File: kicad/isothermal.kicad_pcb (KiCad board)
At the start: 2 copper layers, 62.2 x 49.9 mm, 39 parts, among them P10 CONN_2X1, P40 CONN_2X1, P41 CONN_2X1, P60 CONN_2X1, P70 CONN_6X1, P71 CONN_8X1, P72 CONN_10X1, P73 CONN_8X1, Q1 2N3904, U1 LM324

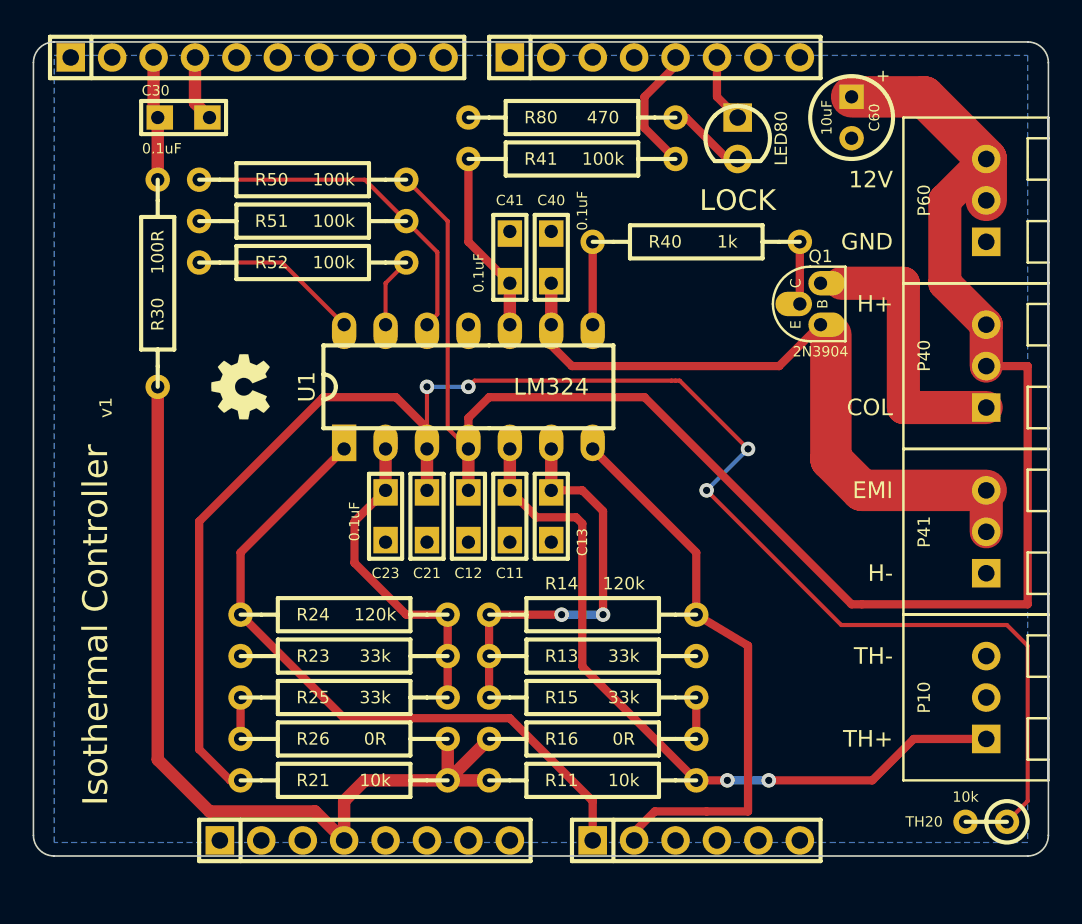
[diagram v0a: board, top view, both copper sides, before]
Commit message: increasing terminal block hole size, fixing pin spacing
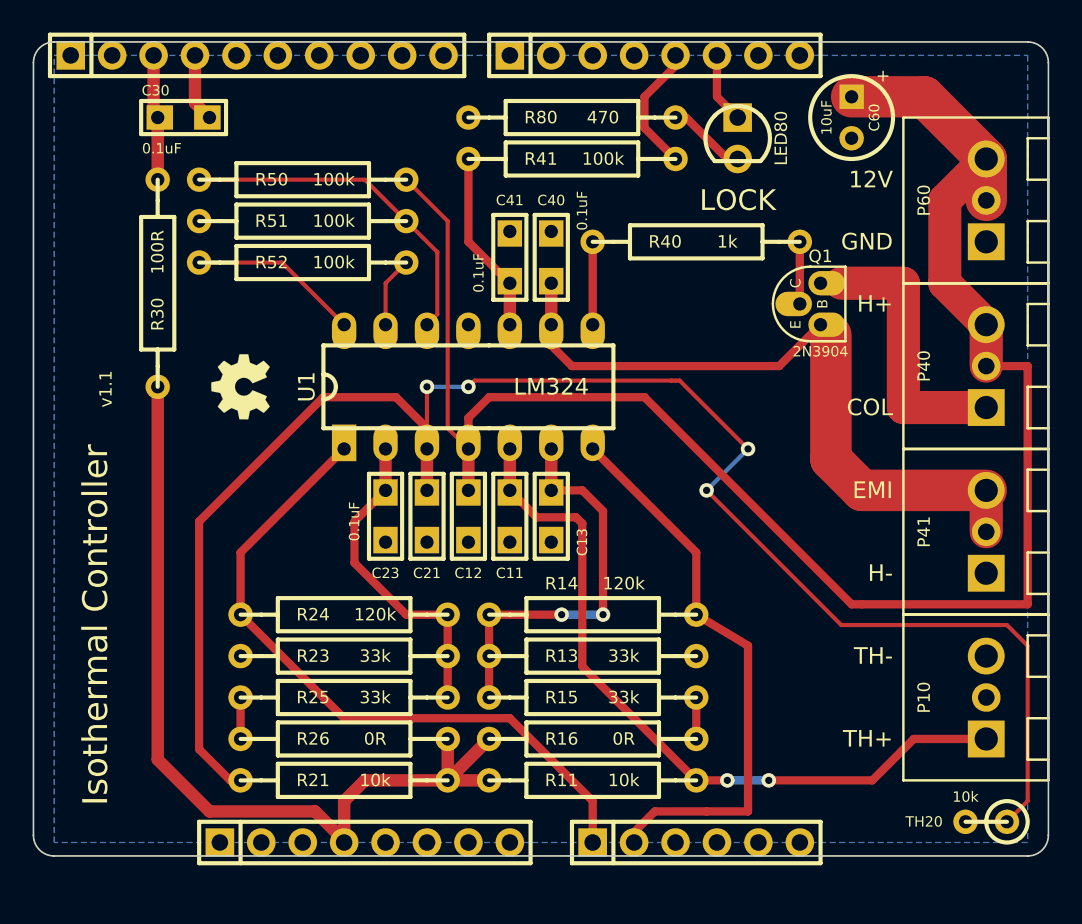
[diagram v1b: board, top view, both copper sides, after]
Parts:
- moved P70 0.13 mm to (210.8, 172.7)
- moved P71 0.13 mm to (188.0, 172.7)
- moved P72 0.13 mm to (178.8, 124.5)
- moved P73 0.13 mm to (205.7, 124.5)
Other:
- board text added: "v1.1"
- board text removed: "v1"

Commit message: v1.1
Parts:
- removed C41: 0.1uF, CERCAP_15_059B_0805
- removed R50, R51, R52: 100k, R_AXIAL_0W25_059A_05_PL
- added C44: 0.1uF, CERCAP_15_059B_0805, F.Cu at (200.7, 127.6)
- added D30: ZENER, DIODE_SS_059A_03_PL, F.Cu at (182.2, 132.1)
- added R31: 330R, R_AXIAL_0W25_059A_PL, F.Cu at (181.0, 146.7)
- added R42: 10k, R_AXIAL_0W25_059A_PL, F.Cu at (189.2, 135.9)
- added R43: 1k, R_AXIAL_0W25_059A_PL, F.Cu at (199.4, 130.8)
- added R44: 100k, R_AXIAL_0W25_059A_PL, F.Cu at (203.2, 127.6)
- C40: value 0.1uF -> 10nF
- Q1: footprint TO-92_Q_EBC_059Bo_PL -> TO-220_V_069A
- R11, R13, R14, R15, R16, R21, R23, R24, R25, R26, R30, R40, R80: footprint R_AXIAL_0W25_059A_05_PL -> R_AXIAL_0W25_059A_PL
- R41: value 100k -> 0R; footprint R_AXIAL_0W25_059A_05_PL -> R_AXIAL_0W25_059A_PL
- moved G*** 26.3 mm to (179.7, 170.2)
- moved R40 11.8 mm to (211.5, 142.9), turned to 90 degrees
- moved Q1 4.26 mm to (220.3, 144.8), turned to 90 degrees
- moved R30 3.70 mm to (178.4, 146.7)
- moved R80 3.17 mm to (203.2, 130.2)
- moved R41 2.84 mm to (199.4, 133.3), turned to 180 degrees
- moved R13 2.54 mm to (212.1, 161.3)
- moved R16 2.54 mm to (212.1, 166.4)
- moved R23 2.54 mm to (189.2, 161.3)
- moved R26 2.54 mm to (189.2, 166.4)
- moved C30 0.90 mm to (181.0, 127.6)
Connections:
- P71 pad 5: (no net) -> 5V
- R11 pad 1: 3V3 -> AREF
- R16 pad 2: 3V3 -> AREF
- R21 pad 1: 3V3 -> AREF
- R26 pad 2: 3V3 -> AREF
- R41 pad 2: D3 -> N-0000036
- U1 pad 14: N-000003 -> N-0000036
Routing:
- net AREF: track 7.60 -> 69.0 mm
- net 5V: track 0.00 -> 33.6 mm
- net 3V3: track 54.3 -> 33.9 mm
- net 12V: track 106.9 -> 88.3 mm
- net N-0000036: track 0.00 -> 12.5 mm
- net N-000003: track 10.5 -> 0.00 mm
- net N-0000055: track 44.2 -> 35.6 mm
- net N-0000033: track 4.34 -> 12.9 mm
- net N-0000040: track 3.81 -> 9.15 mm
- net D3: track 7.80 -> 3.18 mm
- net N-0000031: track 5.08 -> 9.57 mm
- net AGND: track 4.05 -> 8.51 mm
- net A0: track 41.5 -> 37.9 mm
- net N-0000032: track 17.8 -> 14.2 mm
- net N-0000050: track 103.0 -> 99.4 mm, vias 4 -> 5
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
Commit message: v1.1
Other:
- board text added: "B"
- board text added: "C"
- board text added: "E"
- board text removed: "COL"
- board text removed: "EMI"
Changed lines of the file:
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@@
     (links 74)
     (no_connects 2)
-    (area 173.939999 123.584499 236.270001 173.595501)
+    (area 162.706354 121.2088 236.549001 175.9712)
     (thickness 1.6)
-    (drawings 25)
+    (drawings 28)
     (tracks 150)
     (zones 0)
@@
   (layers
     (15 F.Cu signal)
-    (0 B.Cu signal)
+    (0 B.Cu signal hide)
     (16 B.Adhes user)
     (17 F.Adhes user)
@@
       (effects (font (size 0.635 0.635) (thickness 0.127)))
     )
-    (fp_text value 0.1uF (at 0.254 1.905 180) (layer F.SilkS)
+    (fp_text value 0.1uF (at 5.08 0 270) (layer F.SilkS)
       (effects (font (size 0.635 0.635) (thickness 0.127)))
     )
@@
     (descr "TO-220, vertical, 0.04\" holes, 0.069\" pads")
     (tags "TR TO220")
-    (fp_text reference Q1 (at 2.54 2.794 90) (layer F.SilkS)
-      (effects (font (size 0.762 0.762) (thickness 0.1524)))
-    )
-    (fp_text value 2N3904 (at -3.175 0 180) (layer F.SilkS)
+    (fp_text reference Q1 (at 8.89 0 180) (layer F.SilkS)
+      (effects (font (size 0.762 0.762) (thickness 0.1524)))
+    )
+    (fp_text value 2N3904 (at -3.81 0 180) (layer F.SilkS)
       (effects (font (size 0.762 0.762) (thickness 0.1524)))
     )
@@
     )
   )
+  (gr_text C (at 216.535 139.7) (layer F.SilkS)
+    (effects (font (size 0.762 0.762) (thickness 0.1524)))
+  )
+  (gr_text B (at 216.535 142.24) (layer F.SilkS)
+    (effects (font (size 0.762 0.762) (thickness 0.1524)))
+  )
+  (gr_text E (at 216.535 144.78) (layer F.SilkS)
+    (effects (font (size 0.762 0.762) (thickness 0.1524)))
+  )
   (gr_line (start 173.99 124.9045) (end 173.99 172.2755) (angle 90) (layer Edge.Cuts) (width 0.1))
   (gr_line (start 234.95 123.6345) (end 175.26 123.6345) (angle 90) (layer Edge.Cuts) (width 0.1))
@@
     (effects (font (size 1.016 1.016) (thickness 0.2032)) (justify right))
   )
-  (gr_text H+ (at 226.695 139.7) (layer F.SilkS)
+  (gr_text H+ (at 226.695 140.97) (layer F.SilkS)
     (effects (font (size 1.016 1.016) (thickness 0.2032)) (justify right))
   )
-  (gr_text COL (at 226.695 146.05) (layer F.SilkS)
+  (gr_text C (at 226.695 146.05) (layer F.SilkS)
     (effects (font (size 1.016 1.016) (thickness 0.2032)) (justify right))
   )
-  (gr_text EMI (at 226.695 151.13) (layer F.SilkS)
+  (gr_text E (at 226.695 151.13) (layer F.SilkS)
     (effects (font (size 1.016 1.016) (thickness 0.2032)) (justify right))
   )

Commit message: v1.2
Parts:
- removed R16, R26: 0R, R_AXIAL_0W25_059A_PL
- removed R43: 1k, R_AXIAL_0W25_059A_PL
- removed TH20: 10k, R_AXIAL_0W25_V_059A_PL
- added P20: CONN_2X1, TERMINAL_BLOCK_2_5mm, F.Cu at (232.4, 168.9)
- moved R21 26.9 mm to (226.1, 165.1)
- moved R11 25.0 mm to (226.1, 162.6), turned to 180 degrees
- moved P10 5.08 mm to (232.4, 158.8)
- moved P40 5.08 mm to (232.4, 138.4)
- moved P41 5.08 mm to (232.4, 148.6)
- moved P60 5.08 mm to (232.4, 128.3)
- moved R23 2.84 mm to (188.0, 158.8)
- moved R24 2.84 mm to (198.1, 161.3)
- moved R13 2.54 mm to (212.1, 158.8)
- moved R14 2.54 mm to (201.9, 161.3)
- moved R25 1.27 mm to (198.1, 163.8)
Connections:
- C11 pad 1: N-0000048 -> N-0000039
- C21 pad 1: N-0000050 -> N-0000041
- P10 pad 1: N-0000048 -> N-0000039
- P10 pad 2: GND -> AREF
- R11 pad 1: AREF -> N-0000039
- R11 pad 2: N-0000048 -> GND
- R15 pad 2: N-0000035 -> AREF
- R21 pad 1: AREF -> N-0000041
- R21 pad 2: N-0000050 -> GND
- R25 pad 2: N-0000030 -> AREF
- R41 pad 2: N-0000036 (its old number) -> N-0000026
- U1 pad 13: N-0000033 -> N-0000026
- U1 pad 14: N-0000036 (its old number) -> N-0000026
- U1 pad 3: N-0000050 -> N-0000041
- U1 pad 5: N-0000048 -> N-0000039
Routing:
- net N-0000050: track 99.4 -> 0.00 mm, vias 5 -> 0
- net N-0000041: track 0.00 -> 55.1 mm, vias 0 -> 4
- net N-0000048: track 46.8 -> 0.00 mm, vias 2 -> 0
- net AREF: track 69.0 -> 110.7 mm, vias 0 -> 2
- net N-0000039: track 0.00 -> 39.6 mm
- net N-0000033: track 12.9 -> 0.00 mm
- net N-0000036 (its old number): track 12.5 -> 0.00 mm
- net N-0000026: track 0.00 -> 9.94 mm
- net A1: track 34.2 -> 27.3 mm
- net N-0000040: track 24.7 -> 19.9 mm, vias 2 -> 0
- net 12V: track 88.3 -> 85.5 mm
- net N-0000035: track 2.54 -> 0.00 mm
- net N-0000030: track 2.54 -> 0.00 mm
- net A0: track 37.9 -> 39.9 mm
- net N-0000043: track 14.2 -> 12.6 mm
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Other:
- board text added: "3.3V"
- board text added: "5V"
- board text added: "Isothermal Shield"
- board text added: "L+"
- board text added: "L-"
- board text added: "LOAD"
- board text added: "S+"
- board text added: "S-"
- board text added: "SHUNT"
- board text added: "TH1"
- board text added: "TH1+"
- board text added: "TH1-"
- board text added: "TH2"
- board text added: "TH2+"
- board text added: "TH2-"
- board text added: "THERMISTOR"
- board text added: "v1.2"
- board text removed: "H+"
- board text removed: "H-"
- board text removed: "Isothermal Controller"
- board text removed: "TH+"
- board text removed: "TH-"
- board text removed: "v1.1"
